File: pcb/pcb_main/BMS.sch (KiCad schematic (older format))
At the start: 26 parts, among them Q1 PZT3906, SW2 SW_SPDT, U4 MCP73833, U5 LM8364-2.2, U6 LTC3525-5

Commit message: First pass at split pcb design completed
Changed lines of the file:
@@
 $Descr A4 11693 8268
 encoding utf-8
-Sheet 2 3
+Sheet 2 2
 Title ""
 Date ""
@@
 USB_GND
 $Comp
-L Keyboard_Parts:GND #PWR0133
+L Keeb-rescue:GND-Keyboard_Parts-Keeb-rescue #PWR0133
 U 1 1 5D83F92E
 P 2350 6550
@@
 	3800 6000 3800 6150
 $Comp
-L Keyboard_Parts:GND #PWR0134
+L Keeb-rescue:GND-Keyboard_Parts-Keeb-rescue #PWR0134
 U 1 1 5D8BCB19
 P 3800 6550
@@
 	2000 5650 2100 5650
 $Comp
-L Keyboard_Parts:GND #PWR0140
+L Keeb-rescue:GND-Keyboard_Parts-Keeb-rescue #PWR0140
 U 1 1 5D8CEEB4
 P 7600 6000
@@
 	4300 1100 4300 1350
 $Comp
-L Keyboard_Parts:GND #PWR0154
+L Keeb-rescue:GND-Keyboard_Parts-Keeb-rescue #PWR0154
 U 1 1 5DB1497F
 P 4300 2650
@@
 	10400 2850 10050 2850
 $Comp
-L Keyboard_Parts:GND #PWR0128
+L Keeb-rescue:GND-Keyboard_Parts-Keeb-rescue #PWR0128
 U 1 1 5DA21149
 P 9650 2450
@@
 	750  1100 3350 1100
 $Comp
-L Keyboard_Parts:GND #PWR0136
+L Keeb-rescue:GND-Keyboard_Parts-Keeb-rescue #PWR0136
 U 1 1 5DB1A682
 P 9900 3700
@@
 $EndComp
 Wire Wire Line
-	5000 1000 5150 1000
-Wire Wire Line
-	5150 1000 5150 900
-$Comp
-L Keyboard_Parts:GND #PWR0138
+	5000 1200 5150 1200
+Wire Wire Line
+	5150 1200 5150 1300
+$Comp
+L Keeb-rescue:GND-Keyboard_Parts-Keeb-rescue #PWR0138
 U 1 1 5DAEF921
-P 5150 900
-F 0 "#PWR0138" H 5150 950 20  0001 C CNN
-F 1 "GND" H 5150 800 30  0000 C CNN
-F 2 "" H 5150 900 60  0000 C CNN
-F 3 "" H 5150 900 60  0000 C CNN
-	1    5150 900
-	1    0    0    1
-$EndComp
-Wire Wire Line
-	5000 1200 5450 1200
-Wire Wire Line
-	5450 1200 5450 2750
+P 5150 1300
+F 0 "#PWR0138" H 5150 1350 20  0001 C CNN
+F 1 "GND" H 5150 1200 30  0000 C CNN
+F 2 "" H 5150 1300 60  0000 C CNN
+F 3 "" H 5150 1300 60  0000 C CNN
+	1    5150 1300
+	1    0    0    -1
+$EndComp
 Connection ~ 6800 4700
 Wire Wire Line
@@
 	1    0    0    -1
 $EndComp
+Wire Wire Line
+	5450 1000 5000 1000
+Wire Wire Line
+	5450 1000 5450 2750
 $EndSCHEMATC

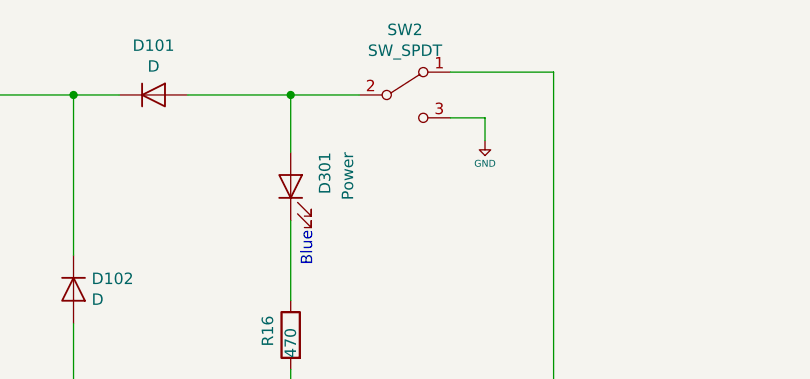
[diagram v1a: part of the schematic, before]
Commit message: Updated connection method on main pcb
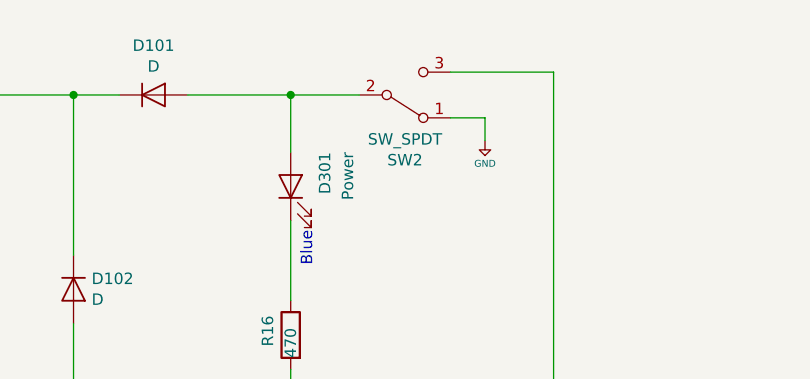
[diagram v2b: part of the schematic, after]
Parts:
- SW2: footprint SVastaCustomParts:400BWMSP1R2BLKSM6QE‎_rocker_switch -> SVastaCustomParts:SW_Slide_C&K_JS102011SAQN
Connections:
- net +5V: now also SW2.1 (A); no longer SW2.3 (C)
- net 5Vbat: now also SW2.3 (C); no longer SW2.1 (A)
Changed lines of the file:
@@
 Wire Wire Line
 	5800 5300 6000 5300
-$Comp
-L Device:D D102
-U 1 1 5DAEE077
-P 3350 1950
-F 0 "D102" V 3304 2029 50  0000 L CNN
-F 1 "D" V 3395 2029 50  0000 L CNN
-F 2 "SVastaCustomParts:D_MiniMELF_Handsoldering_Shorter_Pads" H 3350 1950 50  0001 C CNN
-F 3 "~" H 3350 1950 50  0001 C CNN
-	1    3350 1950
-	0    1    1    0
-$EndComp
 Wire Wire Line
 	3350 2100 3350 3400
 Wire Wire Line
 	3350 1800 3350 1100
-$Comp
-L Device:D D101
-U 1 1 5DAF9F52
-P 3700 1100
-F 0 "D101" H 3700 1316 50  0000 C CNN
-F 1 "D" H 3700 1225 50  0000 C CNN
-F 2 "SVastaCustomParts:D_MiniMELF_Handsoldering_Shorter_Pads" H 3700 1100 50  0001 C CNN
-F 3 "~" H 3700 1100 50  0001 C CNN
-	1    3700 1100
-	1    0    0    -1
-$EndComp
 Wire Wire Line
 	3550 1100 3350 1100
@@
 F 0 "SW2" H 4800 1385 50  0000 C CNN
 F 1 "SW_SPDT" H 4800 1294 50  0000 C CNN
-F 2 "SVastaCustomParts:400BWMSP1R2BLKSM6QE‎_rocker_switch" H 4800 1100 50  0001 C CNN
-F 3 "https://www.digikey.com/product-detail/en/400BWMSP1R2BLKSM6QE/EG4336CT-ND/668634/?itemSeq=322026415" H 4800 1100 50  0001 C CNN
+F 2 "SVastaCustomParts:SW_Slide_C&K_JS102011SAQN" H 4800 1100 50  0001 C CNN
+F 3 "https://dznh3ojzb2azq.cloudfront.net/products/Slide/JS/documents/datasheet.pdf" H 4800 1100 50  0001 C CNN
 	1    4800 1100
-	1    0    0    -1
+	1    0    0    1
 $EndComp
 Wire Wire Line
@@
 Wire Wire Line
 	5450 1000 5450 2750
+$Comp
+L Device:D D102
+U 1 1 5DAEE077
+P 3350 1950
+F 0 "D102" V 3304 2029 50  0000 L CNN
+F 1 "D" V 3395 2029 50  0000 L CNN
+F 2 "SVastaCustomParts:D_MiniMELF_Handsoldering_Shorter_Pads" H 3350 1950 50  0001 C CNN
+F 3 "~" H 3350 1950 50  0001 C CNN
+	1    3350 1950
+	0    1    1    0
+$EndComp
+$Comp
+L Device:D D101
+U 1 1 5DAF9F52
+P 3700 1100
+F 0 "D101" H 3700 1316 50  0000 C CNN
+F 1 "D" H 3700 1225 50  0000 C CNN
+F 2 "SVastaCustomParts:D_MiniMELF_Handsoldering_Shorter_Pads" H 3700 1100 50  0001 C CNN
+F 3 "~" H 3700 1100 50  0001 C CNN
+	1    3700 1100
+	1    0    0    -1
+$EndComp
 $EndSCHEMATC

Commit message: bms changes
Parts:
- removed C10, C11: 1uF, Capacitor_SMD:C_0805_2012Metric_Pad1.15x1.40mm_HandSolder, symbol Device:C
- removed D101, D102: D, SVastaCustomParts:D_MiniMELF_Handsoldering_Shorter_Pads, symbol Device:D
- removed D201: Power Good, LED_SMD:LED_0805_2012Metric_Pad1.15x1.40mm_HandSolder, symbol Device:LED
- removed D202: Charge Complete, LED_SMD:LED_0805_2012Metric_Pad1.15x1.40mm_HandSolder, symbol Device:LED
- removed D203: Charging, LED_SMD:LED_0805_2012Metric_Pad1.15x1.40mm_HandSolder, symbol Device:LED
- removed Q1: PZT3906, Package_TO_SOT_SMD:SOT-223, symbol Transistor_BJT:PZT3906
- removed R10, R17: 10K, Resistor_SMD:R_0805_2012Metric_Pad1.15x1.40mm_HandSolder, symbol Device:R
- removed R11, R12, R13: 470, Resistor_SMD:R_0805_2012Metric_Pad1.15x1.40mm_HandSolder, symbol Device:R
- removed R9: 1K, Resistor_SMD:R_0805_2012Metric_Pad1.15x1.40mm_HandSolder, symbol Device:R
- removed U4: MCP73833, SVastaCustomParts:MCP73833T-AMI-UN, symbol SVastaCustomParts:MCP73833
- added U7: TCK108AF, symbol SVastaCustomParts:TCK108AF
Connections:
- net +5V: now also U7.2 (GND); no longer R16.2, SW2.1 (A)
- net USB_V+: now also SW2.1 (A), U7.3 (Control)
- net Vbat: now also U7.1 (Vout)
- net Vcc: now also SW2.2 (B)
- net at D301.2 (A): no longer SW2.2 (B)
- net Vcharge: no longer names the net of BT1.1 (+)
- net Vcharge: now also U7.5 (Vin)
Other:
- note removed: "Charger"
- note removed: "Green"
- note removed: "Red"
- note removed: "Typical Application from datasheet"
- note removed: "Yellow"
- moved on the sheet: D301, R16
